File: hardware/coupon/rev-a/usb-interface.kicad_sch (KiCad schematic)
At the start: 13 parts, among them J1 USB4505-03-0-A, U29 TLV75533PDBVR, U31 TUSB320LAIRWBR, U32 TS3USB31ERSER, U33 TPD4E05U06DQAR

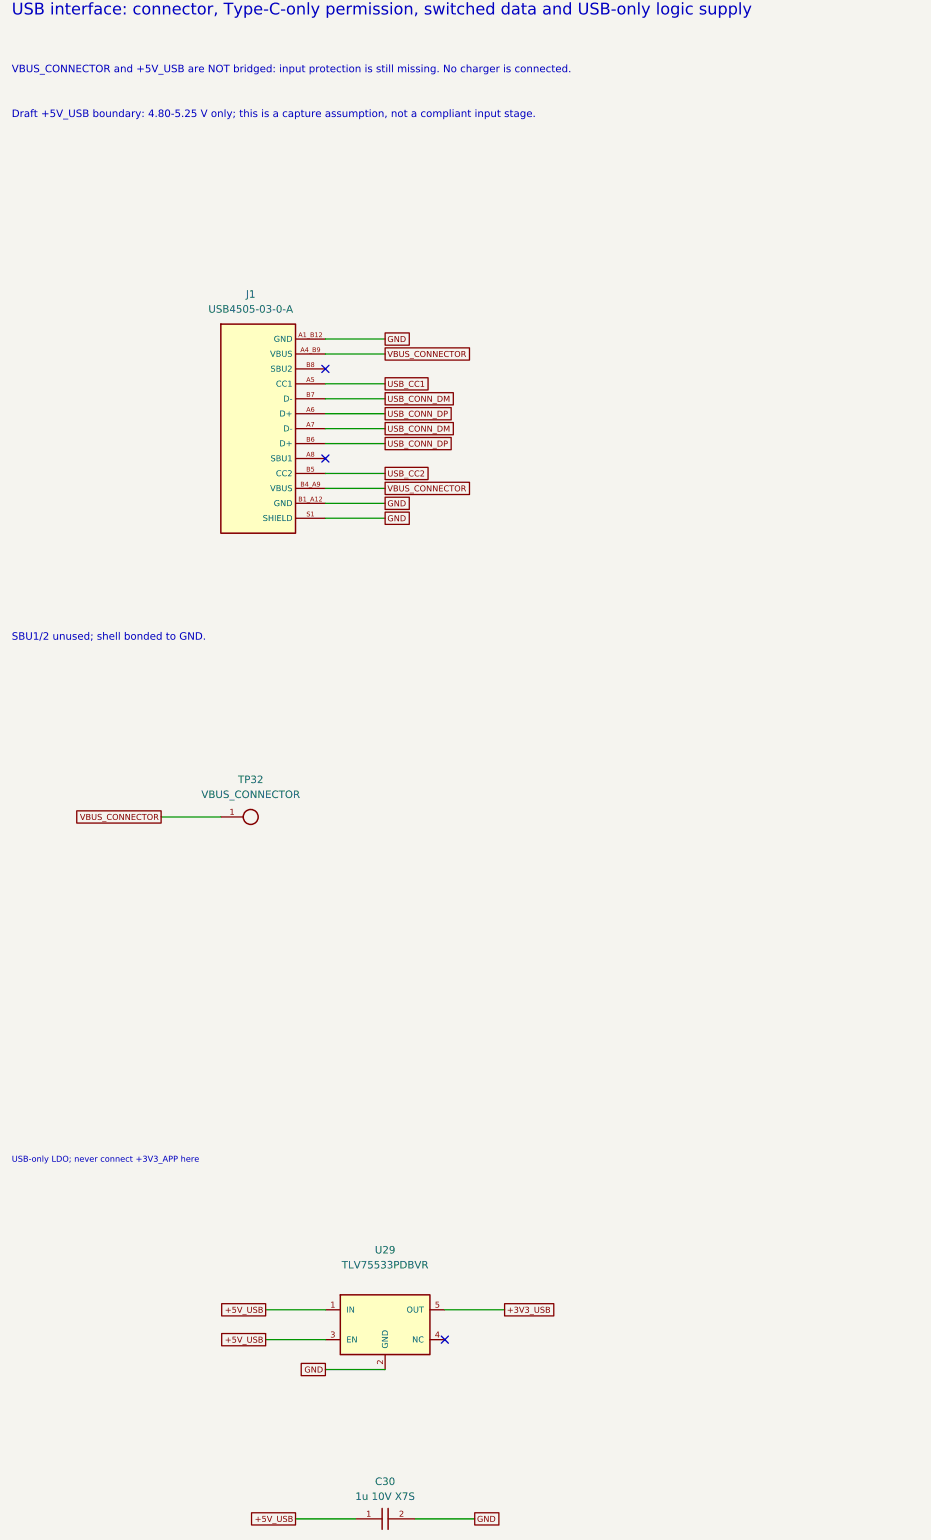
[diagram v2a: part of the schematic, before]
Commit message: Correct USB voltage envelope and widen USB logic supply headroom
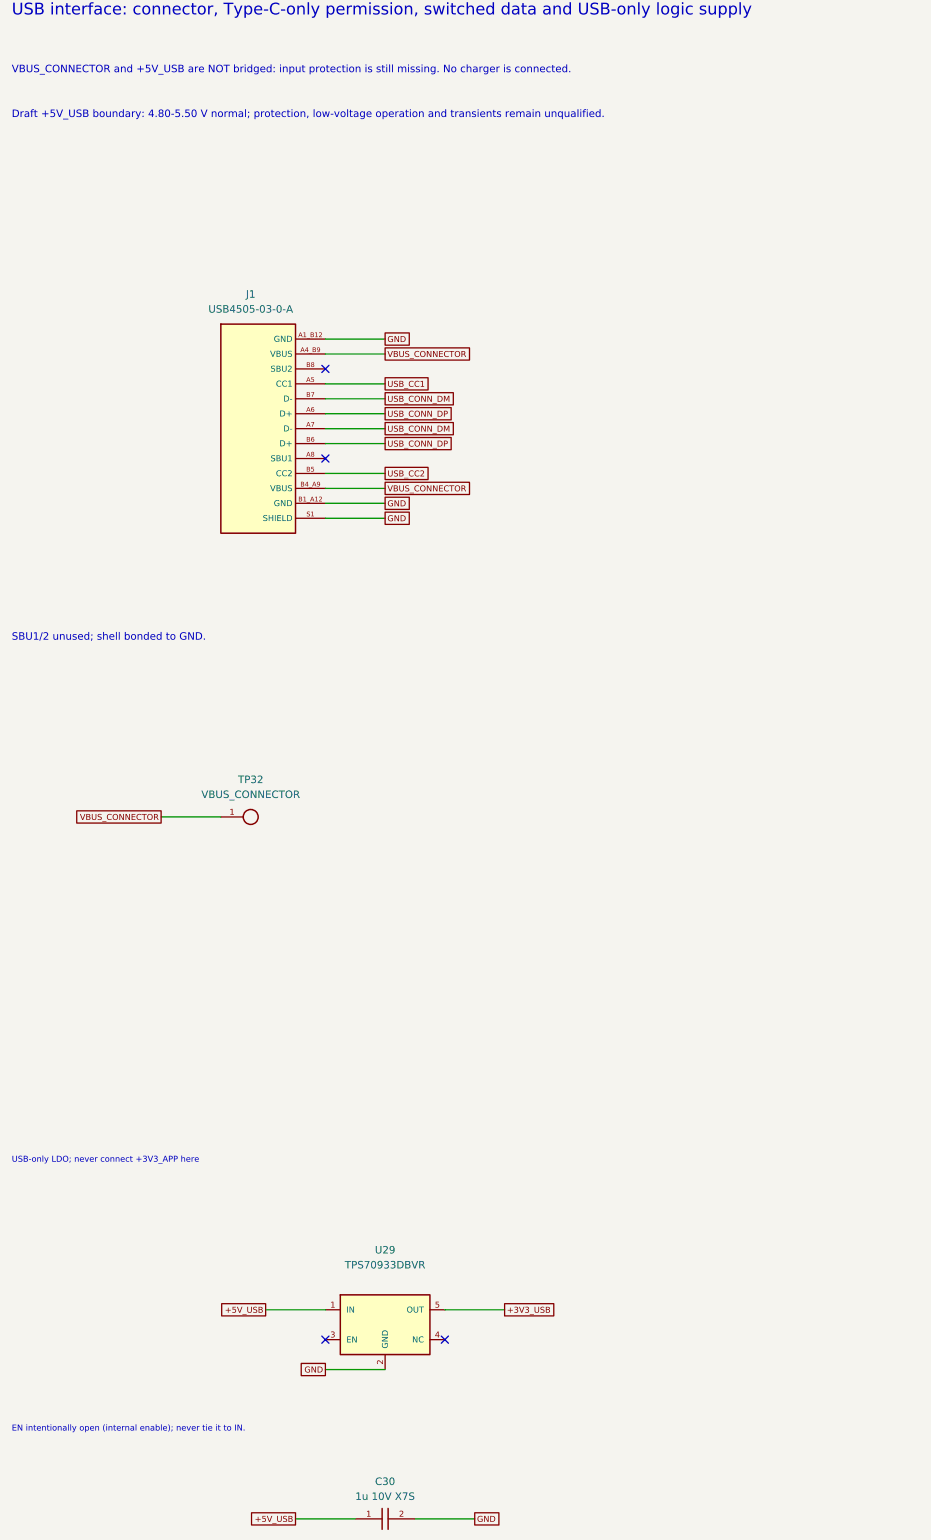
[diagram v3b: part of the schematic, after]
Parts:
- U29: value TLV75533PDBVR -> TPS70933DBVR; symbol rgb-badge-coupon:TLV75533PDBVR -> rgb-badge-coupon:TPS70933DBVR; MPN TLV75533PDBVR -> TPS70933DBVR
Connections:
- net +5V_USB: no longer U29.3 (EN)
- no-connect marks 11 -> 12
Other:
- note added: "Draft +5V_USB boundary: 4.80-5.50 V normal; protection, low-voltage operation and transients remain unqualified."
- note added: "EN intentionally open (internal enable); never tie it to IN."
- note removed: "Draft +5V_USB boundary: 4.80-5.25 V only; this is a capture assumption, not a compliant input stage."
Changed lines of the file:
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@@
 (text "USB interface: connector, Type-C-only permission, switched data and USB-only logic supply" (at 20.320 20.320 0) (effects (font (size 2 2)) (justify left)))
 (text "VBUS_CONNECTOR and +5V_USB are NOT bridged: input protection is still missing. No charger is connected." (at 20.320 30.480 0) (effects (font (size 1.27 1.27)) (justify left)))
-(text "Draft +5V_USB boundary: 4.80-5.25 V only; this is a capture assumption, not a compliant input stage." (at 20.320 38.100 0) (effects (font (size 1.27 1.27)) (justify left)))
+(text "Draft +5V_USB boundary: 4.80-5.50 V normal; protection, low-voltage operation and transients remain unqualified." (at 20.320 38.100 0) (effects (font (size 1.27 1.27)) (justify left)))
 (symbol (lib_id "rgb-badge-coupon:USB4505-03-0-A") (at 60.960 91.440 0) (unit 1)
 (exclude_from_sim no) (in_bom yes) (on_board yes) (dnp no)
@@
 (text "No external CC Rd: detector provides dead-battery Rd." (at 391.160 187.960 0) (effects (font (size 1.016 1.016)) (justify left)))
 (text "USB-only LDO; never connect +3V3_APP here" (at 20.320 215.900 0) (effects (font (size 1.016 1.016)) (justify left)))
-(symbol (lib_id "rgb-badge-coupon:TLV75533PDBVR") (at 83.820 243.840 0) (unit 1)
+(symbol (lib_id "rgb-badge-coupon:TPS70933DBVR") (at 83.820 243.840 0) (unit 1)
 (exclude_from_sim no) (in_bom yes) (on_board yes) (dnp no)
 (property "Reference" "U29" (at 83.820 231.140 0) (effects (font (size 1.27 1.27))))
-(property "Value" "TLV75533PDBVR" (at 83.820 233.680 0) (effects (font (size 1.27 1.27))))
+(property "Value" "TPS70933DBVR" (at 83.820 233.680 0) (effects (font (size 1.27 1.27))))
 (property "Footprint" "rgb-badge-coupon:SOT23_TI_DBV0005A" (at 83.820 243.840 0) (effects (font (size 1.27 1.27)) (hide yes)))
-(property "Datasheet" "https://www.ti.com/lit/ds/symlink/tlv755p.pdf" (at 83.820 243.840 0) (effects (font (size 1.27 1.27)) (hide yes)))
+(property "Datasheet" "https://www.ti.com/lit/ds/symlink/tps709.pdf" (at 83.820 243.840 0) (effects (font (size 1.27 1.27)) (hide yes)))
 (property "Manufacturer" "Texas Instruments" (at 83.820 243.840 0) (effects (font (size 1.27 1.27)) (hide yes)))
-(property "MPN" "TLV75533PDBVR" (at 83.820 243.840 0) (effects (font (size 1.27 1.27)) (hide yes)))
+(property "MPN" "TPS70933DBVR" (at 83.820 243.840 0) (effects (font (size 1.27 1.27)) (hide yes)))
 (pin "1")
 (pin "2")
@@
 (wire (pts (xy 83.820 251.460) (xy 73.660 251.460)) (stroke (width 0) (type default)))
 (global_label "GND" (shape passive) (at 73.660 251.460 180) (effects (font (size 1.016 1.016)) (justify right)) (property "Intersheetrefs" "${INTERSHEET_REFS}" (at 73.660 251.460 0) (effects (font (size 1.27 1.27)) (hide yes))))
-(wire (pts (xy 73.660 246.380) (xy 63.500 246.380)) (stroke (width 0) (type default)))
-(global_label "+5V_USB" (shape passive) (at 63.500 246.380 180) (effects (font (size 1.016 1.016)) (justify right)) (property "Intersheetrefs" "${INTERSHEET_REFS}" (at 63.500 246.380 0) (effects (font (size 1.27 1.27)) (hide yes))))
+(no_connect (at 73.660 246.380))
 (no_connect (at 93.980 246.380))
 (wire (pts (xy 93.980 241.300) (xy 104.140 241.300)) (stroke (width 0) (type default)))
 (global_label "+3V3_USB" (shape passive) (at 104.140 241.300 0) (effects (font (size 1.016 1.016)) (justify left)) (property "Intersheetrefs" "${INTERSHEET_REFS}" (at 104.140 241.300 0) (effects (font (size 1.27 1.27)) (hide yes))))
+(text "EN intentionally open (internal enable); never tie it to IN." (at 20.320 261.620 0) (effects (font (size 1.016 1.016)) (justify left)))
 (symbol (lib_id "rgb-badge-coupon:GRM155C71A105KE11D") (at 83.820 276.860 0) (unit 1)
 (exclude_from_sim no) (in_bom yes) (on_board yes) (dnp no)

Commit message: Normalize Panasonic ERJ order codes across coupon
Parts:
- R71: symbol rgb-badge-coupon:ERJ-2RKF8873X -> rgb-badge-coupon:ERJ2RKF8873X; MPN ERJ-2RKF8873X -> ERJ2RKF8873X
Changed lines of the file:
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@@
 (global_label "+3V3_USB" (shape passive) (at 459.740 81.280 0) (effects (font (size 1.016 1.016)) (justify left)) (property "Intersheetrefs" "${INTERSHEET_REFS}" (at 459.740 81.280 0) (effects (font (size 1.27 1.27)) (hide yes))))
 (text "PORT low = UFP; ADDR NC = GPIO; EN_N low." (at 391.160 127.000 0) (effects (font (size 1.016 1.016)) (justify left)))
-(symbol (lib_id "rgb-badge-coupon:ERJ-2RKF8873X") (at 449.580 147.320 0) (unit 1)
+(symbol (lib_id "rgb-badge-coupon:ERJ2RKF8873X") (at 449.580 147.320 0) (unit 1)
 (exclude_from_sim no) (in_bom yes) (on_board yes) (dnp no)
 (property "Reference" "R71" (at 449.580 140.970 0) (effects (font (size 1.27 1.27))))
@@
 (property "Datasheet" "https://industrial.panasonic.com/cdbs/www-data/pdf/RDA0000/AOA0000C304.pdf" (at 449.580 147.320 0) (effects (font (size 1.27 1.27)) (hide yes)))
 (property "Manufacturer" "Panasonic" (at 449.580 147.320 0) (effects (font (size 1.27 1.27)) (hide yes)))
-(property "MPN" "ERJ-2RKF8873X" (at 449.580 147.320 0) (effects (font (size 1.27 1.27)) (hide yes)))
+(property "MPN" "ERJ2RKF8873X" (at 449.580 147.320 0) (effects (font (size 1.27 1.27)) (hide yes)))
 (pin "1")
 (pin "2")
